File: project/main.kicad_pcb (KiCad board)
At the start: 6 copper layers, 160 x 257 mm, 193 parts

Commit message: adding power cable runs
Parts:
- added L26: light, -local:light_square, B.Cu at (96.3, 75.3)
- added L27: light, -local:light_square, B.Cu at (96.3, 220.3)
- added L28: light, -local:light_square, B.Cu at (96.3, 100.3)
- added L47: light, -local:light_long, B.Cu at (179.3, 123.3)
- added L48: light, -local:light_long, B.Cu at (164.3, 123.3)
- added L49: light, -local:light_long, B.Cu at (149.3, 123.3)
- added L50: light, -local:light_long, B.Cu at (133.3, 123.3)
- added L51: light, -local:light_long, B.Cu at (119.3, 123.3)
- added L52: light, -local:light_long, B.Cu at (179.3, 171.3)
- added L53: light, -local:light_long, B.Cu at (164.3, 171.3)
- added L54: light, -local:light_long, B.Cu at (149.3, 171.3)
- added L55: light, -local:light_long, B.Cu at (134.3, 171.3)
- added L56: light, -local:light_long, B.Cu at (119.3, 171.3)
- added L57: light, -local:light_long, B.Cu at (103.3, 171.3)
- added L58: light, -local:light_long, B.Cu at (98.3, 63.3)
- moved R37 117.6 mm to (82.3, 122.3), turned to 90 degrees
- moved R34 103.7 mm to (197.8, 171.3), turned to 180 degrees
- moved L46 85.0 mm to (96.3, 147.3), turned to 90 degrees
- moved R58 74.6 mm to (148.0, 60.3), turned to 0 degrees
- moved R33 65.0 mm to (201.3, 105.3), turned to -90 degrees
- moved L44 60.1 mm to (126.3, 147.3), turned to 90 degrees
- moved L43 49.2 mm to (141.3, 147.3), turned to -90 degrees
- moved L40 41.4 mm to (186.3, 147.3), turned to 90 degrees
- moved L42 36.1 mm to (156.3, 147.3), turned to 90 degrees
- moved R28 20.3 mm to (200.3, 96.3)
- moved R32 19.8 mm to (199.5, 74.3)
- moved R44 19.4 mm to (100.3, 130.8), turned to -90 degrees
- moved R49 19.4 mm to (107.3, 118.3)
- moved L41 15.3 mm to (171.3, 147.3), turned to 90 degrees
- moved L14 15.0 mm to (111.3, 100.3)
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- renumbered L26 to L29, L27 to L30, L28 to L31, L29 to L32, L30 to L33, L31 to L34, L32 to L35, L33 to L36, L34 to L37, L35 to L38, L36 to L39, L37 to L40, L38 to L41, L39 to L42, L40 to L43, L41 to L44, L42 to L45, L43 to L46, R101 to R100, R102 to R101, R103 to R102, R104 to R103, R105 to R104, R53 to R52, R54 to R53, R55 to R54, R56 to R55, R57 to R56, R58 to R57, R59 to R58, R60 to R59, R61 to R60, R62 to R61, R63 to R62, R64 to R63, R65 to R64, R66 to R65, R67 to R66, R68 to R67, R69 to R68, R70 to R69, R71 to R70, R72 to R71, R73 to R72, R74 to R73, R75 to R74, R76 to R75, R77 to R76, R78 to R77, R79 to R78, R80 to R79, R81 to R80, R82 to R81, R83 to R82, R84 to R83, R85 to R84, R86 to R85, R87 to R86, R88 to R87, R89 to R88, R90 to R89, R91 to R90, R92 to R91, R93 to R92, R94 to R93, R95 to R94, R96 to R95, R97 to R96, R98 to R97, R99 to R98, R100 to R99
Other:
- board text added: "101"
- board text added: "102"
- board text added: "11"
- board text added: "12"
- board text added: "13"
- board text added: "15"
- board text added: "16"
- board text added: "17"
- board text added: "18"
- board text added: "19"
- board text added: "1f socket junction box 3f socket switch light light junction ethernet"
- board text added: "20"
- board text added: "21"
- board text added: "22"
- board text added: "23"
- board text added: "24"
- board text added: "25"
- board text added: "26"
- board text added: "27"
- board text added: "28"
- board text added: "29"
- board text added: "30"
- board text added: "31"
- board text added: "32"
- board text added: "33"
- board text added: "34"
- board text added: "36"
- board text added: "37"
- board text added: "38"
- board text added: "39"
- board text added: "3x1 11m sens via P221 x1"
- board text added: "3x1 11m sens via P321 x1"
- board text added: "3x1 11m sens via P421 x1"
- board text added: "3x1 11m sens x1 via P221"
- board text added: "3x1 11m sens x1 via P321"
- board text added: "3x1 11m sens x1 via P421"
- board text added: "3x1 12m sens via P121 x1"
- board text added: "3x1 12m sens via P221 x1"
- board text added: "3x1 12m sens via P321 x1"
- board text added: "3x1 12m sens via P421 x1"
- board text added: "3x1 5m via P522 sens x1"
- board text added: "3x1 7m sens via P226 x1"
- board text added: "3x1 8m sens x1 via P121"
- board text added: "3x1 B2 10m sens x1"
- board text added: "3x1 B2 13m sens x1"
- board text added: "3x1 B2 21m sens x1"
- board text added: "3x1 B2 29m sens x1"
- board text added: "3x1 B2 37m sens x1"
- board text added: "3x2.5 10m via 221 4x"
- board text added: "3x2.5 11m via D523 x4"
- board text added: "3x2.5 3m via 226 6x"
- board text added: "3x2.5 3m via D221 6x"
- board text added: "3x2.5 3m via D422 x4"
- board text added: "3x2.5 3m via P524 freezer 2x"
- board text added: "3x2.5 5m via 216 1x"
- board text added: "3x2.5 5m via 217 1x"
- board text added: "3x2.5 5m via D425 x1"
- board text added: "3x2.5 5m via D523 x4"
- board text added: "3x2.5 6m via 226 6x"
- board text added: "3x2.5 6m via D521 x4"
- board text added: "3x2.5 8m via D422 x4 top"
- board text added: "3x2.5 9m via D521 x4"
- board text added: "3x2.5 B10 22m rack x1 top"
- board text added: "3x2.5 B4 15m x2 top"
- board text added: "3x2.5 C16 14m instr x6x5"
- board text added: "3x2.5 C16 16m tools x6x3"
- board text added: "3x2.5 C16 18m"
- board text added: "3x2.5 C16 22m"
- board text added: "3x2.5 C16 23m"
- board text added: "3x2.5 C16 23m 6x"
- board text added: "3x2.5 C16 24m 4x"
- board text added: "3x2.5 C16 27m 6x"
- board text added: "3x2.5 C16 29m 4x"
- board text added: "3x2.5 C16 29m 6x"
- board text added: "3x2.5 C16 29m x1"
- board text added: "3x2.5 C16 30m oven 1x"
- board text added: "3x2.5 C16 30m printers x6"
- board text added: "3x2.5 C16 31m 4x"
- board text added: "3x2.5 C16 31m kettle 6x"
- board text added: "3x2.5 C16 32m"
- board text added: "3x2.5 C16 32m 6x"
- board text added: "3x2.5 C16 36m 6x"
- board text added: "3x2.5 C16 38m 4x"
- board text added: "3x2.5 C16 9m 4x"
- board text added: "3x2.5 C2 37m pump x1"
- board text added: "3x2.5 C4 18m freezer"
- board text added: "3x2.5 via 215 1x 5m"
- board text added: "3x4 C20 27m 4x welders"
- board text added: "3x4 C20 35m 1x top compressor"
- board text added: "40"
- board text added: "43"
- board text added: "44"
- board text added: "46"
- board text added: "49"
- board text added: "5"
- board text added: "555"
- board text added: "5x16 C40 26m"
- board text added: "5x2.5 C16 29m exit fan"
- board text added: "5x2.5 C16 32m 2x"
- board text added: "5x2.5 C16 38m exit fans"
- board text added: "5x2.5 C16 42m fan and heater"
- board text added: "5x4 C20 24m 1x"
- board text added: "5x4 C20 29m 2x"
- board text added: "7"
- board text added: "7x0.75 B2 10m D35A ~D35C"
- board text added: "7x0.75 B2 12m D357 ~D359"
- board text added: "7x0.75 B2 14m"
- board text added: "7x0.75 B2 14m D354 ~D356"
- board text added: "7x0.75 B2 16m"
- board text added: "7x0.75 B2 16m D351 ~D353"
- board text added: "7x0.75 B2 16m D453 ~D456"
- board text added: "7x0.75 B2 17m D451 ~D452"
- board text added: "7x0.75 B2 17m table lights"
- board text added: "7x0.75 B2 18m"
- board text added: "7x0.75 B2 18m screen"
- board text added: "7x0.75 B2 20m"
- board text added: "7x0.75 B2 20m D457 ~D45A"
- board text added: "7x0.75 B2 21m D551 ~D553"
- board text added: "7x0.75 B2 23m"
- board text added: "7x0.75 B2 23m D43B ~D43E"
- board text added: "7x0.75 B2 26m"
- board text added: "7x0.75 B2 27m D152~D153"
- board text added: "7x0.75 B2 29m D554~D555"
- board text added: "7x0.75 B2 34m D154~D156"
- board text added: "7x0.75 B2 7m D35G ~D35I"
- board text added: "7x0.75 B2 8m"
- board text added: "7x0.75 B2 8m D35E ~D35F"
- board text added: "9"
- board text added: "All cables goes here"
- board text added: "D111"
- board text added: "D112"
- board text added: "D113"
- board text added: "D114"
- board text added: "D115"
- board text added: "D131"
- board text added: "D151"
- board text added: "D152"
- board text added: "D153"
- board text added: "D154"
- board text added: "D155"
- board text added: "D156"
- board text added: "D161"
- board text added: "D162"
- board text added: "D211"
- board text added: "D212"
- board text added: "D213"
- board text added: "D214"
- board text added: "D215"
- board text added: "D216"
- board text added: "D217"
- board text added: "D218"
- board text added: "D219"
- board text added: "D21A"
- board text added: "D21B"
- board text added: "D21C"
- board text added: "D221"
- board text added: "D226"
- board text added: "D231"
- board text added: "D241"
- board text added: "D251"
- board text added: "D252"
- board text added: "D253"
- board text added: "D254"
- board text added: "D255"
- board text added: "D256"
- board text added: "D257"
- board text added: "D258"
- board text added: "D259"
- board text added: "D25A"
- board text added: "D25B"
- board text added: "D25C"
- board text added: "D25D"
- board text added: "D25E"
- board text added: "D25F"
- board text added: "D261"
- board text added: "D262"
- board text added: "D263"
- board text added: "D264"
- board text added: "D311"
- board text added: "D312"
- board text added: "D331"
- board text added: "D351"
- board text added: "D352"
- board text added: "D353"
- board text added: "D354"
- board text added: "D355"
- board text added: "D356"
- board text added: "D357"
- board text added: "D358"
- board text added: "D359"
- board text added: "D35A"
- board text added: "D35B"
- board text added: "D35C"
- board text added: "D35D"
- board text added: "D35E"
- board text added: "D35F"
- board text added: "D35G"
- board text added: "D35H"
- board text added: "D35I"
- board text added: "D361"
- board text added: "D362"
- board text added: "D363"
- board text added: "D364"
- board text added: "D365"
- board text added: "D366"
- board text added: "D411"
- board text added: "D412"
- board text added: "D413"
- board text added: "D415"
- board text added: "D421"
- board text added: "D422"
- board text added: "D423"
- board text added: "D424"
- board text added: "D425"
- board text added: "D441"
- board text added: "D451"
- board text added: "D452"
- board text added: "D453"
- board text added: "D454"
- board text added: "D455"
- board text added: "D456"
- board text added: "D457"
- board text added: "D458"
- board text added: "D459"
- board text added: "D45A"
- board text added: "D45B"
- board text added: "D45C"
- board text added: "D45D"
- board text added: "D45E"
- board text added: "D461"
- board text added: "D462"
- board text added: "D463"
- board text added: "D464"
- board text added: "D465"
- board text added: "D511"
- board text added: "D512"
- board text added: "D513"
- board text added: "D514"
- board text added: "D515"
- board text added: "D516"
- board text added: "D521"
- board text added: "D551"
- board text added: "D552"
- board text added: "D553"
- board text added: "D554"
- board text added: "D561"
- board text added: "D562"
- board text added: "P121"
- board text added: "P122"
- board text added: "P123"
- board text added: "P124"
- board text added: "P125"
- board text added: "P211"
- board text added: "P221"
- board text added: "P222"
- board text added: "P223"
- board text added: "P224"
- board text added: "P225"
- board text added: "P226"
- board text added: "P321"
- board text added: "P322"
- board text added: "P323"
- board text added: "P324"
- board text added: "P411"
- board text added: "P421"
- board text added: "P422"
- board text added: "P423"
- board text added: "P424"
- board text added: "P425"
- board text added: "P521"
- board text added: "P522"
- board text added: "P523"
- board text added: "P524"
- board text added: "[source] [room] [type] [number]"
- board text added: "ceiling and height measurements"
- board text added: "source: D - default switched P - permanent U - UPS"
- board text added: "xx1x"
- board text added: "xx2x"
- board text added: "xx3x"
- board text added: "xx4x"
- board text added: "xx5x"
- board text added: "xx6x"
- board text added: "xxx"

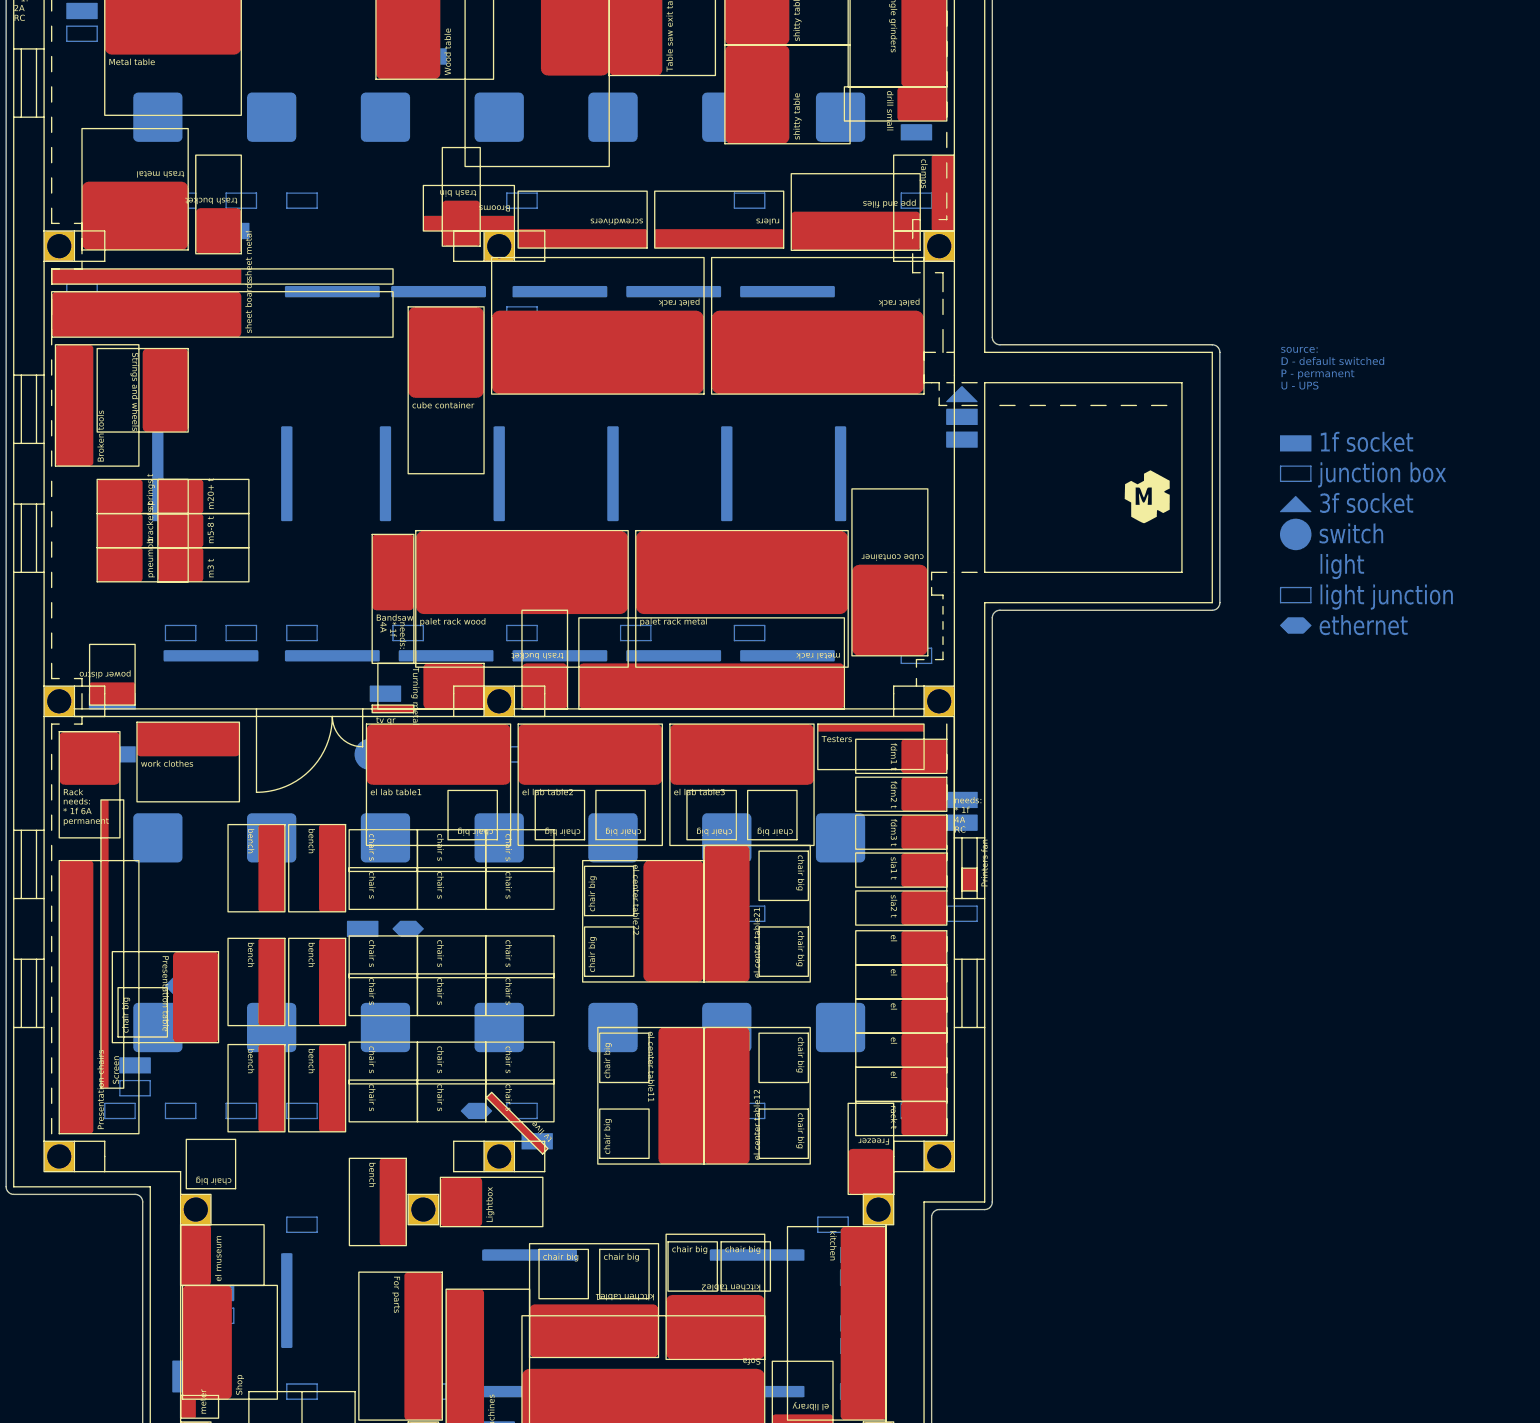
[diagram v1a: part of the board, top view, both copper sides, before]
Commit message: small tweeks and fixes as we implement the plan
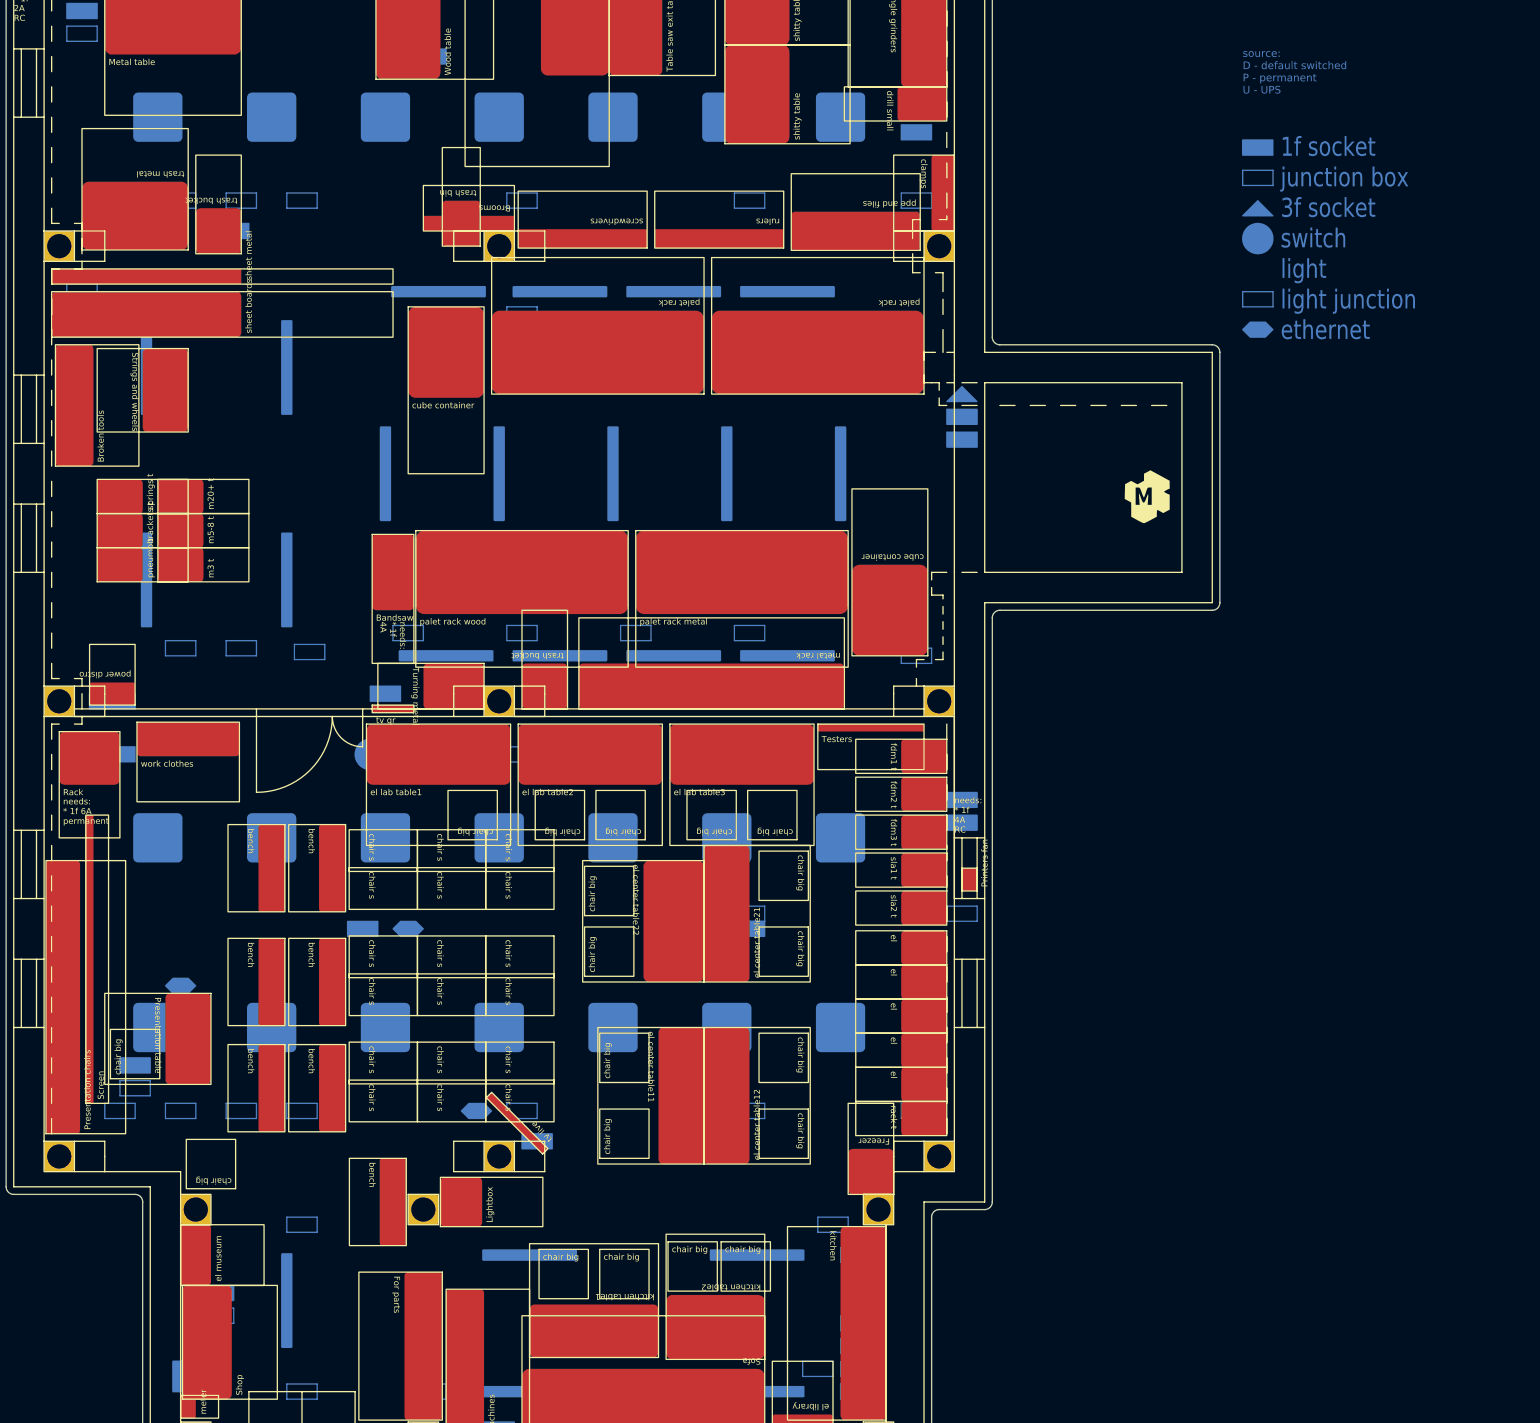
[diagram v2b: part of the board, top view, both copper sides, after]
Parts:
- removed L45: light, -local:light_long
- moved L46 14.1 mm to (94.8, 133.3)
- moved L57 13.1 mm to (94.8, 161.3), turned to -90 degrees
- moved L51 11.7 mm to (113.3, 133.3), turned to -90 degrees
- moved L56 11.7 mm to (113.3, 161.3), turned to -90 degrees
- moved Cb18 5.59 mm to (93.3, 223.8)
- moved R63 5.59 mm to (103.3, 215.8)
- moved R64 2.83 mm to (86.8, 230.3)
- moved R65 1.75 mm to (81.5, 234.3)
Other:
- board text added: "3x1 108m for room 3 lights"
- board text added: "3x1 10m sens via P522 x1"
- board text added: "3x1 20m for room 1 lights"
- board text added: "3x1 24m for room 5 lights"
- board text added: "3x1 80m for room 2 lights"
- board text added: "3x1 80m for room 4 lights"
- board text added: "3x2.5 3m via P524 freezer 1x"
- board text added: "3x2.5 6m via P524 fridge 1x"
- board text added: "3x2.5 B6 22m rack x1 top"
- board text added: "3x2.5 C4 30m printers x6"
- board text added: "555-2"
- board text added: "5x2.5 C2 29m exit fan"
- board text added: "5x2.5 C2 38m exit fans"
- board text added: "5x2.5 C6 42m fan and heater"
- board text added: "7x0.75 B2 7m D35G ~D35H"
- board text added: "D151-1"
- board text added: "D152-2"
- board text added: "D153-3"
- board text added: "D154-1"
- board text added: "D155-2"
- board text added: "D156-3"
- board text added: "D251-1"
- board text added: "D252-2"
- board text added: "D253-1"
- board text added: "D254-2"
- board text added: "D255-3"
- board text added: "D256-4"
- board text added: "D257-1"
- board text added: "D258-2"
- board text added: "D259-3"
- board text added: "D25A-4"
- board text added: "D25B-1"
- board text added: "D25C-2"
- board text added: "D25D-3"
- board text added: "D25E-4"
- board text added: "D351-1"
- board text added: "D352-2"
- board text added: "D353-3"
- board text added: "D354-1"
- board text added: "D355-2"
- board text added: "D356-3"
- board text added: "D357-1"
- board text added: "D358-2"
- board text added: "D359-3"
- board text added: "D35A-1"
- board text added: "D35B-2"
- board text added: "D35C-3"
- board text added: "D35D-1"
- board text added: "D35E-2"
- board text added: "D35F-3"
- board text added: "D35G-1"
- board text added: "D35H-2"
- board text added: "D414"
- board text added: "D416"
- board text added: "D451-1"
- board text added: "D452-2"
- board text added: "D453-1"
- board text added: "D454-2"
- board text added: "D455-3"
- board text added: "D456-4"
- board text added: "D457-1"
- board text added: "D458-2"
- board text added: "D459-3"
- board text added: "D45A-4"
- board text added: "D45B-1"
- board text added: "D45C-2"
- board text added: "D45D-3"
- board text added: "D45E-4"
- board text added: "D551-1"
- board text added: "D552-2"
- board text added: "D553-3"
- board text added: "D554-1"
- board text added: "P511"
- board text added: "P512"
- board text removed: "3x2.5 3m via P524 freezer 2x"
- board text removed: "3x2.5 B10 22m rack x1 top"
- board text removed: "3x2.5 C16 30m printers x6"
- board text removed: "555"
- board text removed: "5x2.5 C16 29m exit fan"
- board text removed: "5x2.5 C16 38m exit fans"
- board text removed: "5x2.5 C16 42m fan and heater"
- board text removed: "7x0.75 B2 7m D35G ~D35I"
- board text removed: "7x0.75 B2 8m"
- board text removed: "D151"
- board text removed: "D152"
- board text removed: "D153"
- board text removed: "D154"
- board text removed: "D155"
- board text removed: "D156"
- board text removed: "D251"
- board text removed: "D252"
- board text removed: "D253"
- board text removed: "D254"
- board text removed: "D255"
- board text removed: "D256"
- board text removed: "D257"
- board text removed: "D258"
- board text removed: "D259"
- board text removed: "D25A"
- board text removed: "D25B"
- board text removed: "D25C"
- board text removed: "D25D"
- board text removed: "D25E"
- board text removed: "D351"
- board text removed: "D352"
- board text removed: "D353"
- board text removed: "D354"
- board text removed: "D355"
- board text removed: "D356"
- board text removed: "D357"
- board text removed: "D358"
- board text removed: "D359"
- board text removed: "D35A"
- board text removed: "D35B"
- board text removed: "D35C"
- board text removed: "D35D"
- board text removed: "D35E"
- board text removed: "D35F"
- board text removed: "D35G"
- board text removed: "D35H"
- board text removed: "D35I"
- board text removed: "D451"
- board text removed: "D452"
- board text removed: "D453"
- board text removed: "D454"
- board text removed: "D455"
- board text removed: "D456"
- board text removed: "D457"
- board text removed: "D458"
- board text removed: "D459"
- board text removed: "D45A"
- board text removed: "D45B"
- board text removed: "D45C"
- board text removed: "D45D"
- board text removed: "D45E"
- board text removed: "D551"
- board text removed: "D552"
- board text removed: "D553"
- board text removed: "D554"

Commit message: adding comunications wiring and naming
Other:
- board text added: "000"
- board text added: "14m projector"
- board text added: "35"
- board text added: "3x1 14m sens via P421 x1 bottom"
- board text added: "3x1 17m sens via P421 x1 bottom"
- board text added: "3x2.5 C16 14m instr x20"
- board text added: "3x2.5 C16 16m tools x20"
- board text added: "3x4 C20 35m 1x compressor"
- board text added: "EL audio 18m"
- board text added: "P412"
- board text added: "P413"
- board text added: "P414"
- board text added: "TV1 18m"
- board text added: "ap-L1 28m"
- board text added: "ap-L2 24m"
- board text added: "ap-L3 15m"
- board text added: "ap-L4 16m"
- board text added: "ap-S2 21m"
- board text added: "ap-S4 21m"
- board text added: "ap-U2 30m"
- board text added: "ap-U4 11m"
- board text added: "cam-el1 11m"
- board text added: "cam-el2 11m"
- board text added: "cam-el3 24m"
- board text added: "cam-purvinos1 21m"
- board text added: "cam-purvinos2 34m"
- board text added: "cam-sandelis1 16m"
- board text added: "cam-staklide1 34m"
- board text added: "el-center1 20m"
- board text added: "el-center2 23m"
- board text added: "el-pc 1-1~1-8 2-1~2-8 x16 16m"
- board text added: "hnt-pc 20m"
- board text added: "laser 40m"
- board text added: "laser-pc 40m"
- board text added: "print-dfm1 19m"
- board text added: "print-dfm2 19m"
- board text removed: "101"
- board text removed: "102"
- board text removed: "3x2.5 C16 14m instr x6x5"
- board text removed: "3x2.5 C16 16m tools x6x3"
- board text removed: "3x4 C20 35m 1x top compressor"
